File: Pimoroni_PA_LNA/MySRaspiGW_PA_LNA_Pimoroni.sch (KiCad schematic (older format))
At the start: 5 parts, among them P1 CONN_02X04, U1 NRF24L01

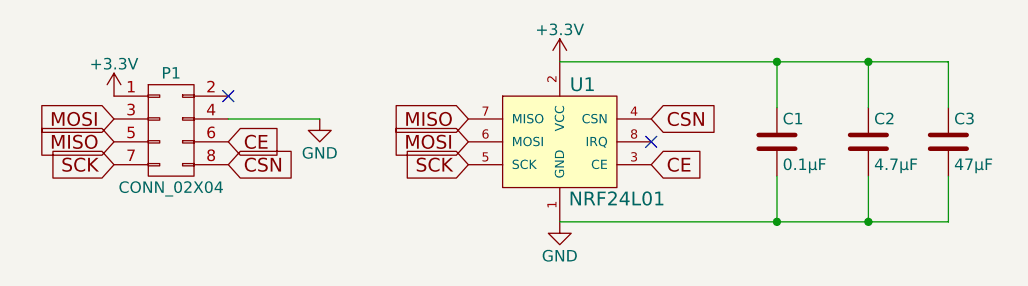
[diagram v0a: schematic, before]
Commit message: v1.1 IRQ support
Added IRQ support on pin 18
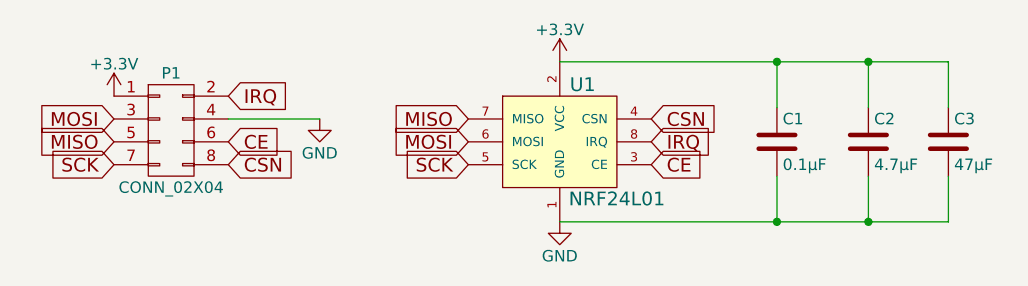
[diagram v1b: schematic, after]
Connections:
- net IRQ: now reaches U1.8 (IRQ)
- net IRQ: now also P1.2 (P2)
- no-connect marks 2 -> 0
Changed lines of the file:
@@
 LIBS:mysensors_security
 LIBS:mysensors_sensors
+LIBS:maxim
+LIBS:MySRaspiGW_PA_LNA_Pimoroni-cache
 EELAYER 25 0
 EELAYER END
@@
 Sheet 1 1
 Title "MySRaspiGW_Pimoroni"
-Date "05/29/2016"
-Rev "1.0"
+Date "03/13/2017"
+Rev "1.1"
 Comp "https://github.com/emc2cube/MySRaspiGW/tree/master/Pimoroni"
 Comment1 ""
@@
 Wire Wire Line
 	4300 1250 4300 1050
-$Comp
-L CONN_02X04 P1
-U 1 1 573ACFFE
-P 1650 1350
-F 0 "P1" H 1650 1600 50  0000 C CNN
-F 1 "CONN_02X04" H 1650 1100 50  0000 C CNN
-F 2 "Socket_Strips:Socket_Strip_Straight_2x04" H 1650 150 50  0001 C CNN
-F 3 "" H 1650 150 50  0000 C CNN
-	1    1650 1350
-	1    0    0    -1
-$EndComp
 $Comp
 L GND #PWR02
@@
 Connection ~ 4300 1050
 Connection ~ 4700 1050
-NoConn ~ 3750 1400
-NoConn ~ 1900 1200
+$Comp
+L CONN_02X04 P1
+U 1 1 573ACFFE
+P 1650 1350
+F 0 "P1" H 1650 1600 50  0000 C CNN
+F 1 "CONN_02X04" H 1650 1100 50  0000 C CNN
+F 2 "Socket_Strips:Socket_Strip_Straight_2x04" H 1650 150 50  0001 C CNN
+F 3 "" H 1650 150 50  0000 C CNN
+	1    1650 1350
+	1    0    0    -1
+$EndComp
+Text GLabel 1900 1200 2    60   Input ~ 0
+IRQ
+Text GLabel 3750 1400 2    60   Input ~ 0
+IRQ
 $EndSCHEMATC
